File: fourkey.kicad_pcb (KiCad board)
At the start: 2 copper layers, 85.3 x 77.7 mm, 23 parts, among them K1 KEYSW, K2 KEYSW, K3 KEYSW, K4 KEYSW, SW1 RESET, U1 ProMicro

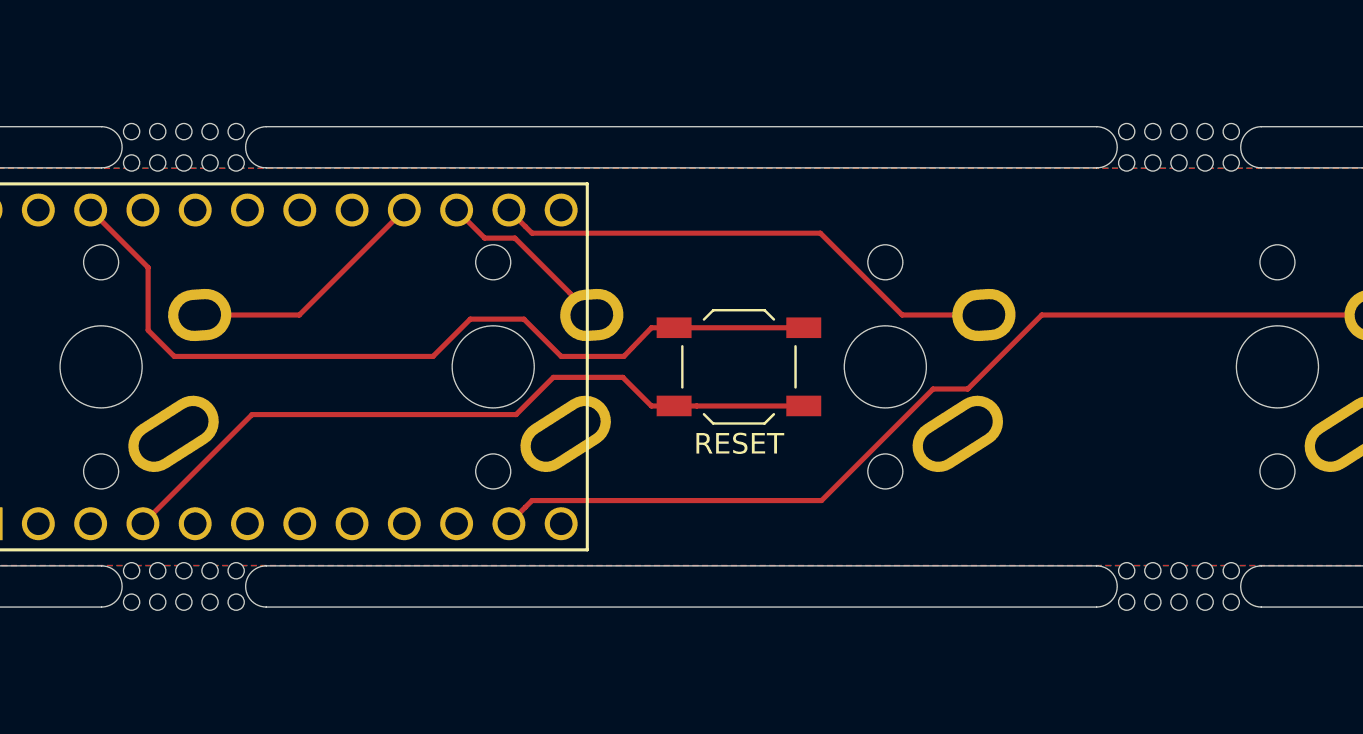
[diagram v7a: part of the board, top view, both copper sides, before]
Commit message: shift mousebites to be less bitey on plates
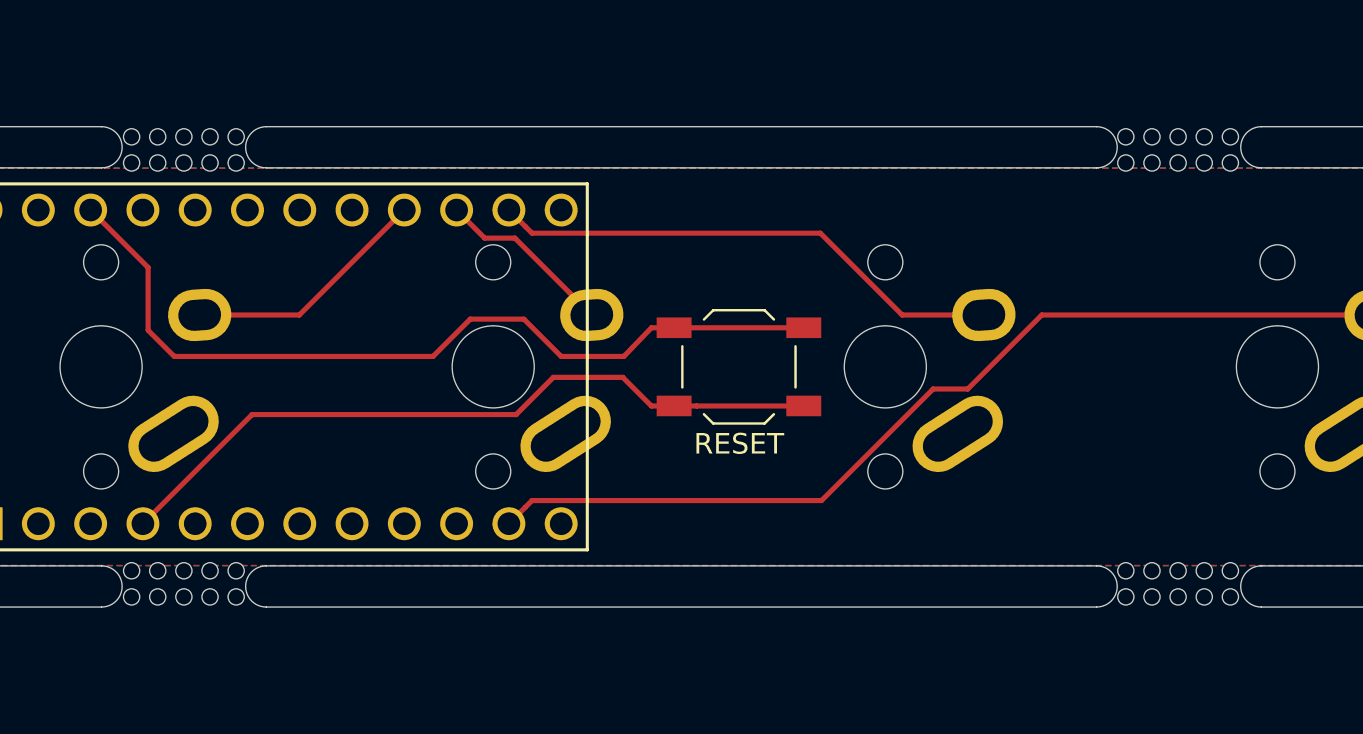
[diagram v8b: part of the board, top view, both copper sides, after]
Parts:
- moved REF** 0.26 mm to (130.3, 90.9)
- moved REF** 0.26 mm to (130.3, 68.1)
- moved REF** 0.25 mm to (82.0, 90.9)
- moved REF** 0.25 mm to (82.0, 68.1)
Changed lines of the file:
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@@
   )
   (module Keebio-Parts:breakaway-mousebites (layer F.Cu)
-    (at 82 91.186)
+    (at 82 90.932)
     (fp_text reference REF** (at 0 -3.048) (layer Dwgs.User) hide
       (effects (font (size 1 1) (thickness 0.15)))
@@
   )
   (module Keebio-Parts:breakaway-mousebites (layer F.Cu)
-    (at 130.344 91.186)
+    (at 130.302 90.932)
     (fp_text reference REF** (at 0 -3.048) (layer Dwgs.User) hide
       (effects (font (size 1 1) (thickness 0.15)))
@@
   )
   (module Keebio-Parts:breakaway-mousebites (layer F.Cu)
-    (at 130.344 67.818 180)
+    (at 130.302 68.072 180)
     (fp_text reference REF** (at 0 -3.048) (layer Dwgs.User) hide
       (effects (font (size 1 1) (thickness 0.15)))
@@
   )
   (module Keebio-Parts:breakaway-mousebites (layer F.Cu)
-    (at 82 67.818 180)
+    (at 82 68.072 180)
     (fp_text reference REF** (at 0 -3.048) (layer Dwgs.User) hide
       (effects (font (size 1 1) (thickness 0.15)))
@@
   )
   (module Keebio-Parts:breakaway-mousebites (layer F.Cu)
-    (at 130.344 69.85)
+    (at 130.302 69.85)
     (fp_text reference REF** (at 0 -3.048) (layer Dwgs.User) hide
       (effects (font (size 1 1) (thickness 0.15)))
@@
   )
   (module Keebio-Parts:breakaway-mousebites (layer F.Cu)
-    (at 130.344 89.154 180)
+    (at 130.302 89.154 180)
     (fp_text reference REF** (at 0 -3.048) (layer Dwgs.User) hide
       (effects (font (size 1 1) (thickness 0.15)))
